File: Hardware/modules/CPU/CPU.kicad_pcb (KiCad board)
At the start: 4 copper layers, 83.3 x 68.2 mm, 16 parts, among them J1 ABORT, J2 SO/MX, J3 Bus_PCI_6502, J5 Bank Bridge A, J6 Bank Bridge B, J7 Bank Bridge C, U1 65C02 / 65816, U2 74LVC1GU04DRL, U3 74HC245, U4 74HC373

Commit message: Update Module Files and Readme
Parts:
- added G***: LOGO, Eigene:logo, F.Cu at (188.6, 78.7)
- added REF**: WEEE-Logo_5.6x8mm_SilkScreen, Symbol:WEEE-Logo_5.6x8mm_SilkScreen, F.Cu at (189.2, 112.4)
- added REF**: ESD-Logo_8.9x8mm_SilkScreen, Symbol:ESD-Logo_8.9x8mm_SilkScreen, F.Cu at (177.2, 78.7)
- added REF**: OSHW-Logo2_9.8x8mm_SilkScreen, Symbol:OSHW-Logo2_9.8x8mm_SilkScreen, F.Cu at (189.2, 101.6)
- added Ref**: Val**, Eigene:ladder_4, F.Cu at (114.9, 69.2)
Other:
- board text added: "6502-Mode: U3 and U4 are DNP Bridge indicated Pins on U3 65816-Mode: U3 = 74HC245 U4 = 74HC373 No bridging at U3"
- board text added: "Jumper Settings: Mode | JP1 | J1 | J2 ------+-------+-------+------ 6502 | open | 1-2 | 1-2 65816 | close | 2-3 | 2-3"
- board text added: "ROM-Bank Buffered Address RAM-Bank"
- board text added: "S65 CPU"
- board text added: "in 65816-Mode bridge as needed"

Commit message: Hardware Update Add MyCPU VGA Module Beautify all Schematics minor Error corrections Readme Update
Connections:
- J3 pad A24: /~{IO} -> unconnected-(J3-~{IO}-PadA24)_0
- J3 pad A25: /~{ROM} -> unconnected-(J3-~{ROM}-PadA25)
- J3 pad A27: /~{IRQ_0.0} -> unconnected-(J3-~{IRQ_0.0}-PadA27)
- J3 pad A28: /~{IRQ_0.1} -> unconnected-(J3-~{IRQ_0.1}-PadA28)
- J3 pad A29: /~{IRQ_0.2} -> unconnected-(J3-~{IRQ_0.2}-PadA29)_0
- J3 pad A30: /~{IRQ_0.3} -> unconnected-(J3-~{IRQ_0.3}-PadA30)
- J3 pad A31: /~{IRQ_0.4} -> unconnected-(J3-~{IRQ_0.4}-PadA31)
- J3 pad A32: /~{IRQ_0.5} -> unconnected-(J3-~{IRQ_0.5}-PadA32)
- J3 pad A33: /~{IRQ_0.6} -> unconnected-(J3-~{IRQ_0.6}-PadA33)
- J3 pad A34: /~{IRQ_0.7} -> unconnected-(J3-~{IRQ_0.7}-PadA34)
- J3 pad B24: /~{L_RAM} -> unconnected-(J3-~{L_RAM}-PadB24)_0
- J3 pad B25: /~{H_RAM} -> unconnected-(J3-~{H_RAM}-PadB25)_0
- J3 pad B28: /~{IRQ_0} -> unconnected-(J3-~{IRQ_0}-PadB28)_0
- J3 pad B29: /~{IRQ_1} -> unconnected-(J3-~{IRQ_1}-PadB29)
- J3 pad B30: /~{IRQ_2} -> unconnected-(J3-~{IRQ_2}-PadB30)_0
- J3 pad B31: /~{IRQ_3} -> unconnected-(J3-~{IRQ_3}-PadB31)_0
- J3 pad B32: /~{IRQ_4} -> unconnected-(J3-~{IRQ_4}-PadB32)_0
- J3 pad B34: /PAGE -> unconnected-(J3-PAGE_ROM-PadB34)_0
- U4 pad 1: unconnected-(U4-OE-Pad1) -> GND

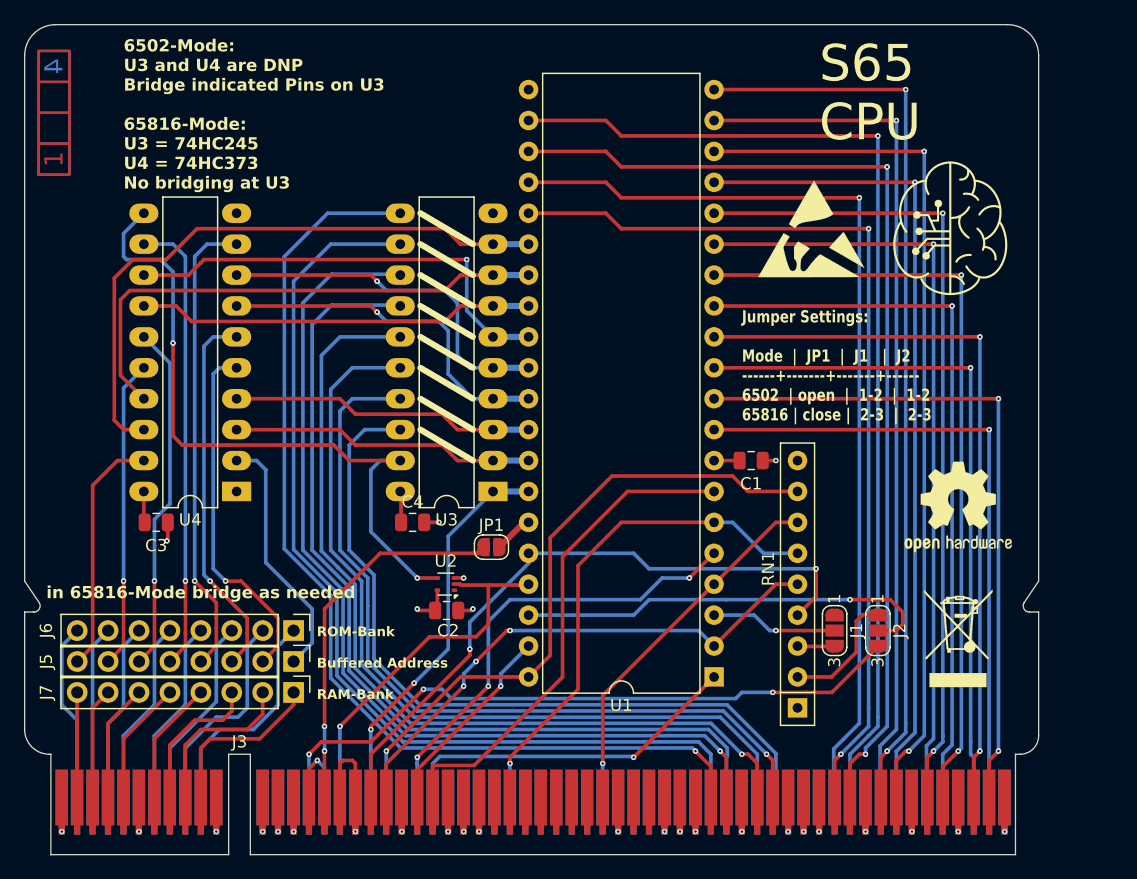
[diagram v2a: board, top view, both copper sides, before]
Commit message: update CPU design to reference WDC design
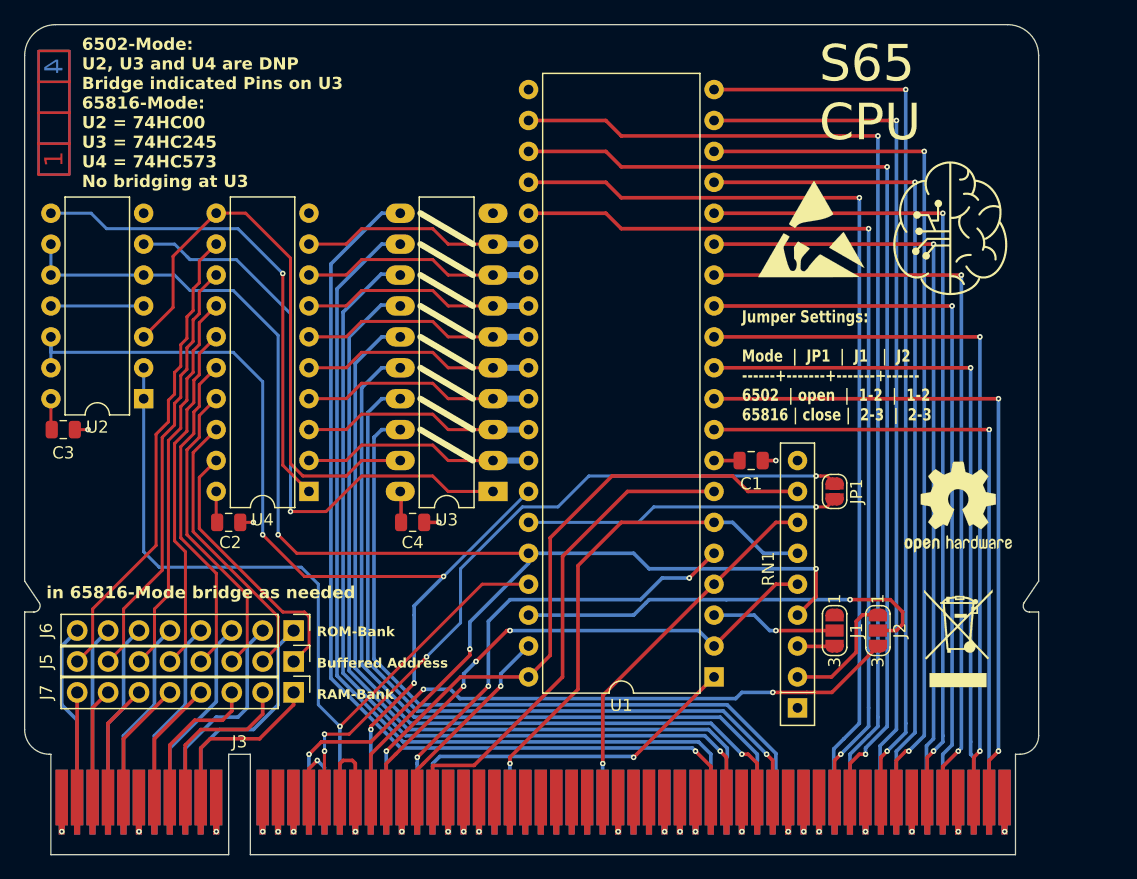
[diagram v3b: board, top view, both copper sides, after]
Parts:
- U2: value 74LVC1GU04DRL -> 74HC00; footprint Package_TO_SOT_SMD:SOT-553 -> Package_DIP:DIP-14_W7.62mm
- U4: value 74HC373 -> 74LS573; footprint Package_DIP:DIP-20_W7.62mm_LongPads -> Package_DIP:DIP-20_W7.62mm
- moved U2 29.1 mm to (122.3, 92.7)
- moved JP1 28.6 mm to (179.1, 100.3), turned to -90 degrees
- moved C2 19.3 mm to (129.3, 102.9)
- moved C3 10.8 mm to (115.7, 95.2)
- moved U4 5.94 mm to (135.9, 100.3)
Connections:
- U2 pad 1: unconnected-(U2-NC-Pad1) -> /CLK
- U2 pad 3: GND -> Net-(U3-CE)
- U2 pad 4: Net-(U3-CE) -> /W/~{R}
- U2 pad 5: +5V -> /~{BE}
- U3 pad 1: /R/~{W} -> Net-(U3-A->B)
- U4 pad 1: GND -> Net-(U4-OE)
- U4 pad 12: /BA4 -> /BA7
- U4 pad 13: Net-(U1-D4) -> /BA6
- U4 pad 14: Net-(U1-D5) -> /BA5
- U4 pad 15: /BA5 -> /BA4
- U4 pad 16: /BA6 -> /BA3
- U4 pad 17: Net-(U1-D6) -> /BA2
- U4 pad 18: Net-(U1-D7) -> /BA1
- U4 pad 19: /BA7 -> /BA0
- U4 pad 2: /BA0 -> Net-(U1-D0)
- U4 pad 3: Net-(U1-D0) -> Net-(U1-D1)
- U4 pad 4: Net-(U1-D1) -> Net-(U1-D2)
- U4 pad 5: /BA1 -> Net-(U1-D3)
- U4 pad 6: /BA2 -> Net-(U1-D4)
- U4 pad 7: Net-(U1-D2) -> Net-(U1-D5)
- U4 pad 8: Net-(U1-D3) -> Net-(U1-D6)
- U4 pad 9: /BA3 -> Net-(U1-D7)
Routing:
- net /~{BE}: track 54.0 -> 114.9 mm, vias 2 -> 3
- net Net-(U3-A->B): track 0.00 -> 49.4 mm, vias 0 -> 1
- net /R/~{W}: track 32.2 -> 81.6 mm, vias 2 -> 4
- net Net-(U4-OE): track 0.00 -> 39.9 mm, vias 0 -> 1
- net /CLK: track 30.9 -> 69.2 mm
- net Net-(U1-D7): track 50.7 -> 19.1 mm
- net /E: track 30.7 -> 58.8 mm, vias 2 -> 4
- net Net-(U1-D6): track 43.3 -> 19.1 mm
- net Net-(JP1-B): track 3.24 -> 25.9 mm, vias 0 -> 1
- net /BA7: track 20.2 -> 39.0 mm
- net Net-(U1-D4): track 37.2 -> 19.1 mm, vias 1 -> 0
- net Net-(U1-D5): track 32.7 -> 19.1 mm
- net /BA3: track 38.4 -> 27.1 mm, vias 1 -> 0
- net Net-(U1-D3): track 29.7 -> 19.1 mm, vias 1 -> 0
- net Net-(U1-D2): track 29.2 -> 19.1 mm, vias 1 -> 0
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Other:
- board text added: "6502-Mode: U2, U3 and U4 are DNP Bridge indicated Pins on U3 65816-Mode: U2 = 74HC00 U3 = 74HC245 U4 = 74HC573 No bridging at U3"
- board text removed: "6502-Mode: U3 and U4 are DNP Bridge indicated Pins on U3 65816-Mode: U3 = 74HC245 U4 = 74HC373 No bridging at U3"

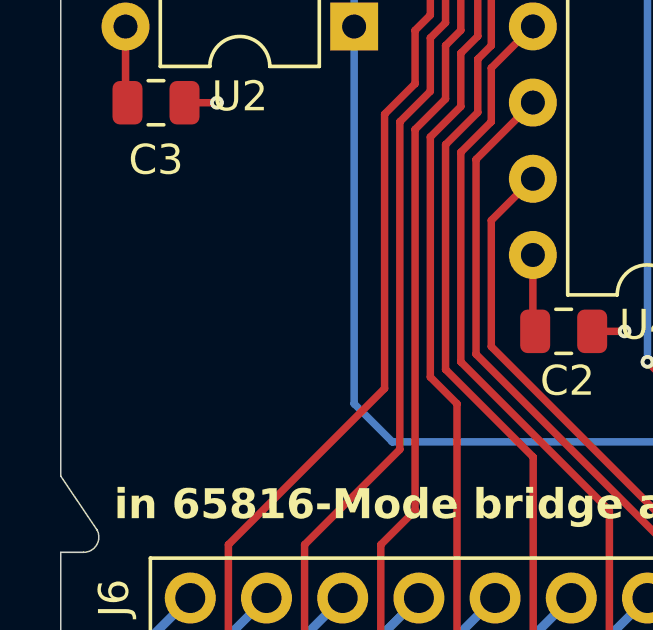
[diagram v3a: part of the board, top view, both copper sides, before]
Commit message: Hardware Review Pt. 1 fix Address Decoding for Strobe Generators add bulk capacitance to every board fix wiring of Prototyping Board
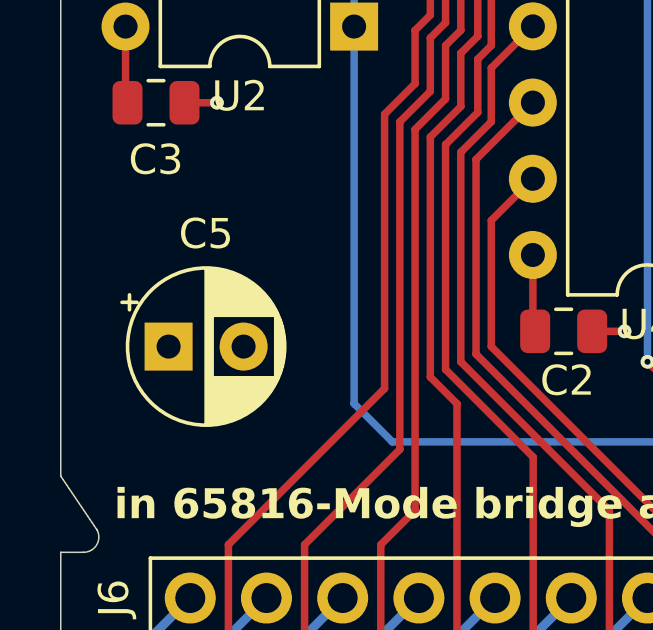
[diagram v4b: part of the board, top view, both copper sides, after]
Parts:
- added C5: 10µ, Capacitor_THT:CP_Radial_D5.0mm_P2.50mm, F.Cu at (116.1, 103.4)

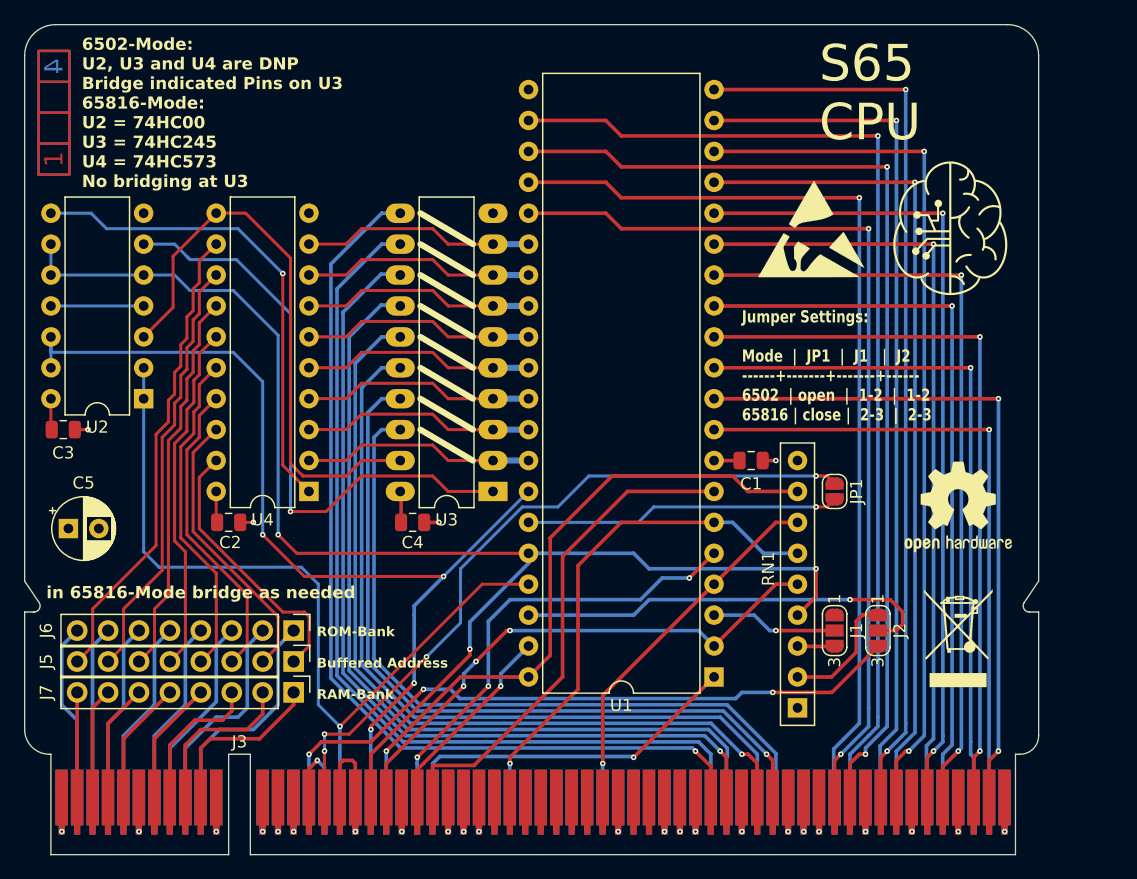
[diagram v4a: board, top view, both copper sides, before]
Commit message: Big Review Update - Changed Copper Pours on all PCBs - Implemented errors found at review - fixed some additional errors
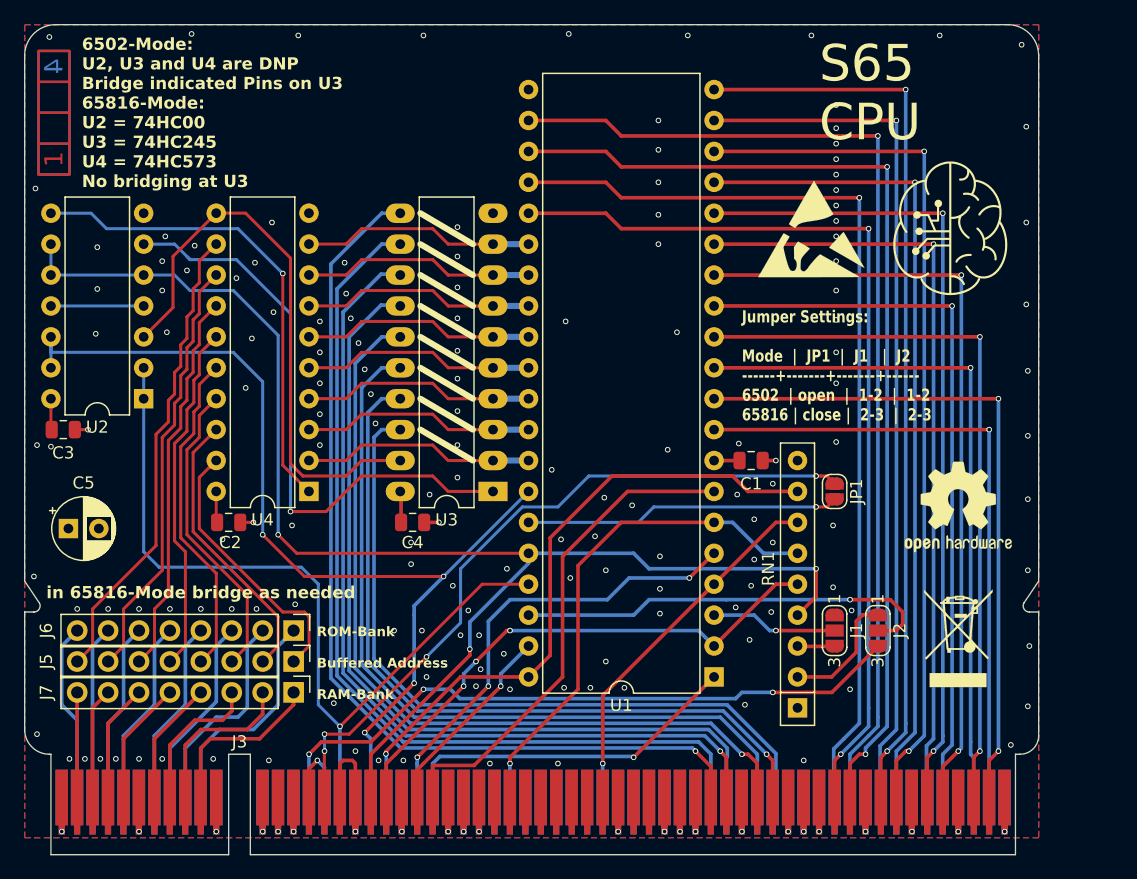
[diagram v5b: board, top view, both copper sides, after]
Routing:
- net +5V: vias 4 -> 157
- added copper zone on B.Cu, net +5V
- added copper zone on F.Cu, net +5V
- added copper zone on In1.Cu, net GND
- removed copper zone on In1.Cu, net +5V
